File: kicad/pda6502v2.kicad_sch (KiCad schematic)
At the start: 87 parts, among them J1 GPIO1, J2 GPIO2, J3 UART, J4 Screw_Terminal_01x02, J5 Conn_02x04_Odd_Even, J6 ICSP, J7 SPI, J8 FPGA_EXT, J9 SID, SW1 SW_Push, SW2 SW_Push, U1 W65C02SxP, U10 LT3030, U11 SC28L92A1B, U2 W65C22SxP, U3 W65C22SxP, U4 DS1818, U5 AS6C4008-55PCN, U6 ARMSID, U7 AT25M01, U8 ICE40HX4K-TQ144, U9 TLV1117-33, X1 8 MHz, X2 3.6864 MHz

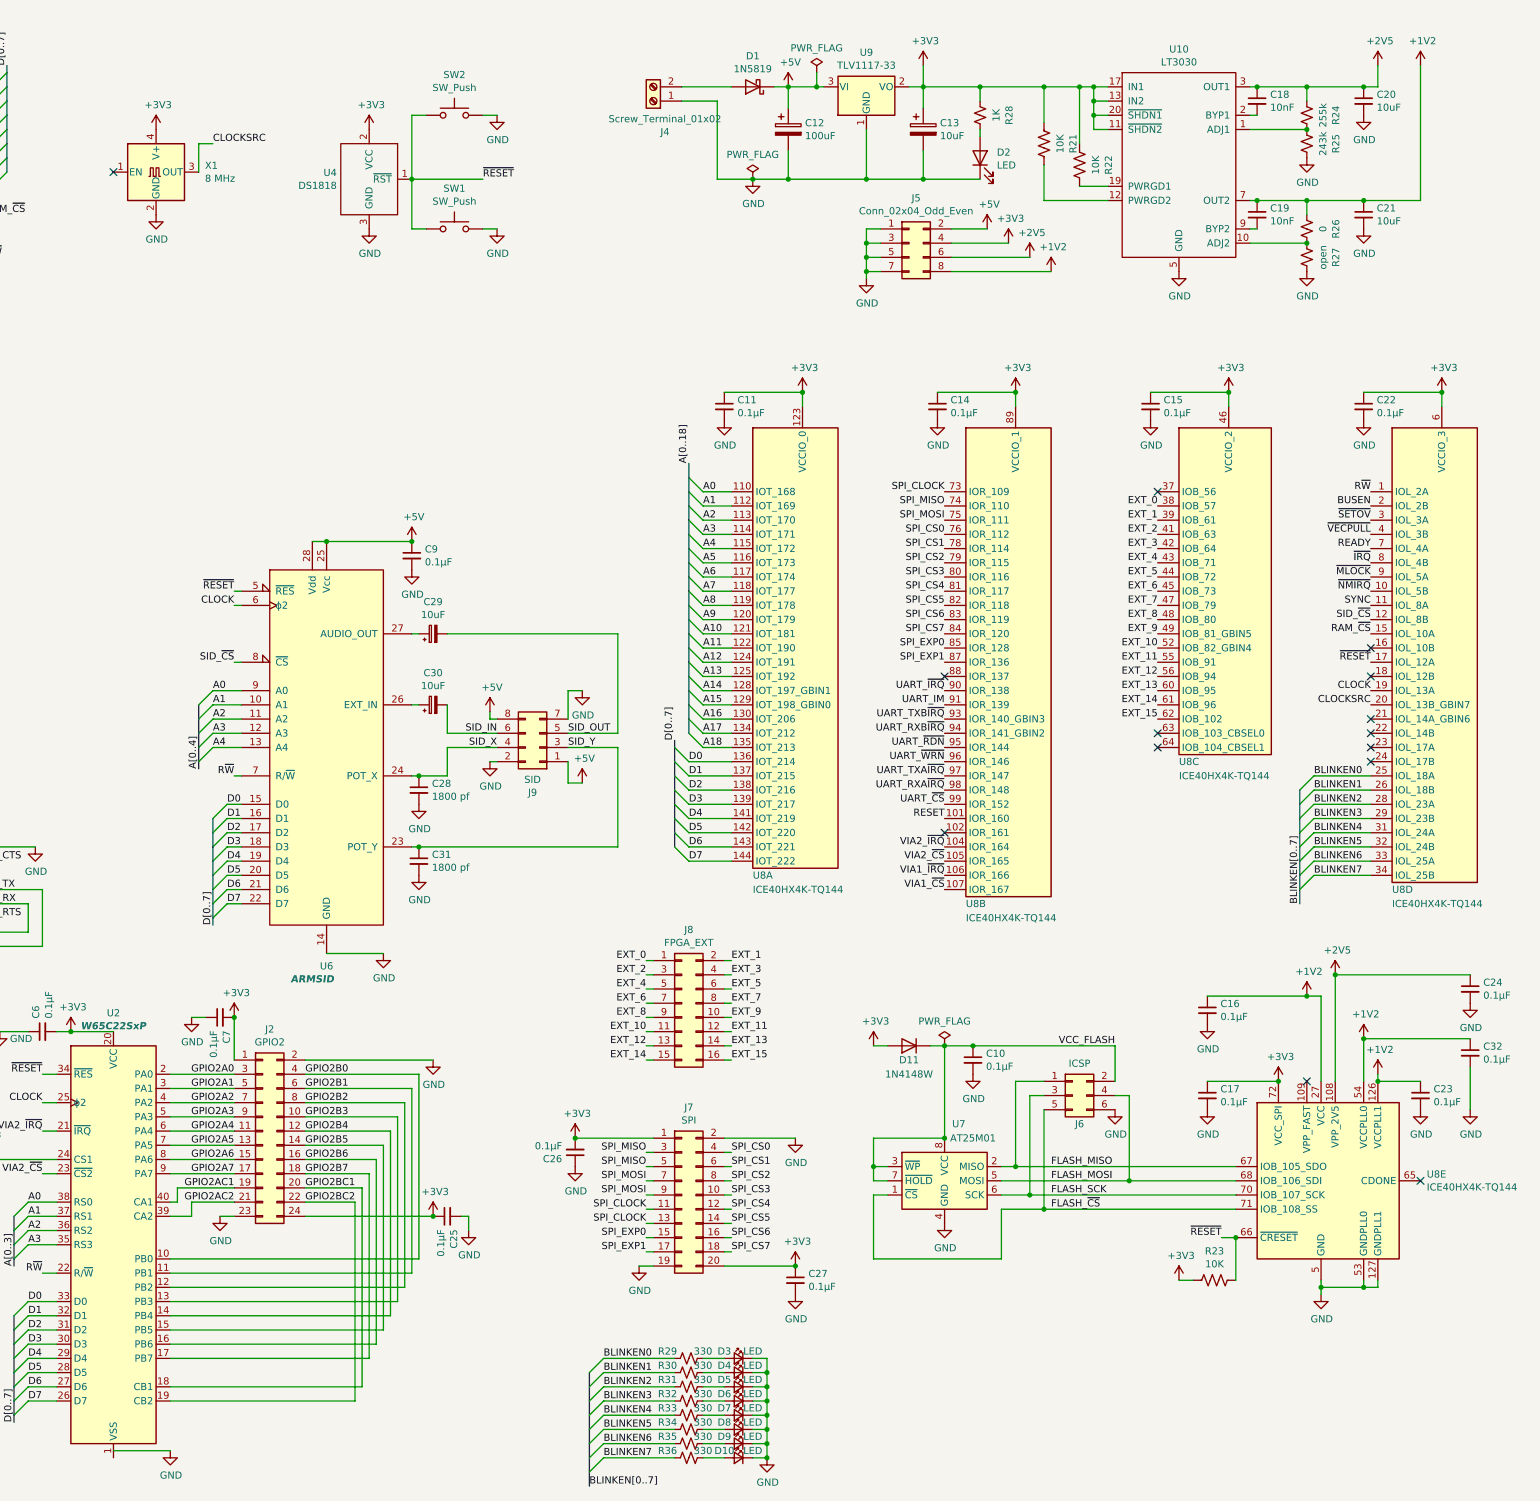
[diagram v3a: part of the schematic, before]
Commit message: kicad: schematic Electrical Rules Checker all fixed
Mostly involved unstacking invisible duplicate power pins on the LM3030
vreg, because the labels (IN1, IN2) of the invisible power pins get
inherited by the net connected to +3V3 which causes the net to have
multiple names; a harmless warning.

The four GND pins can stay invisible-stacked because they have the same
name as the GND net.
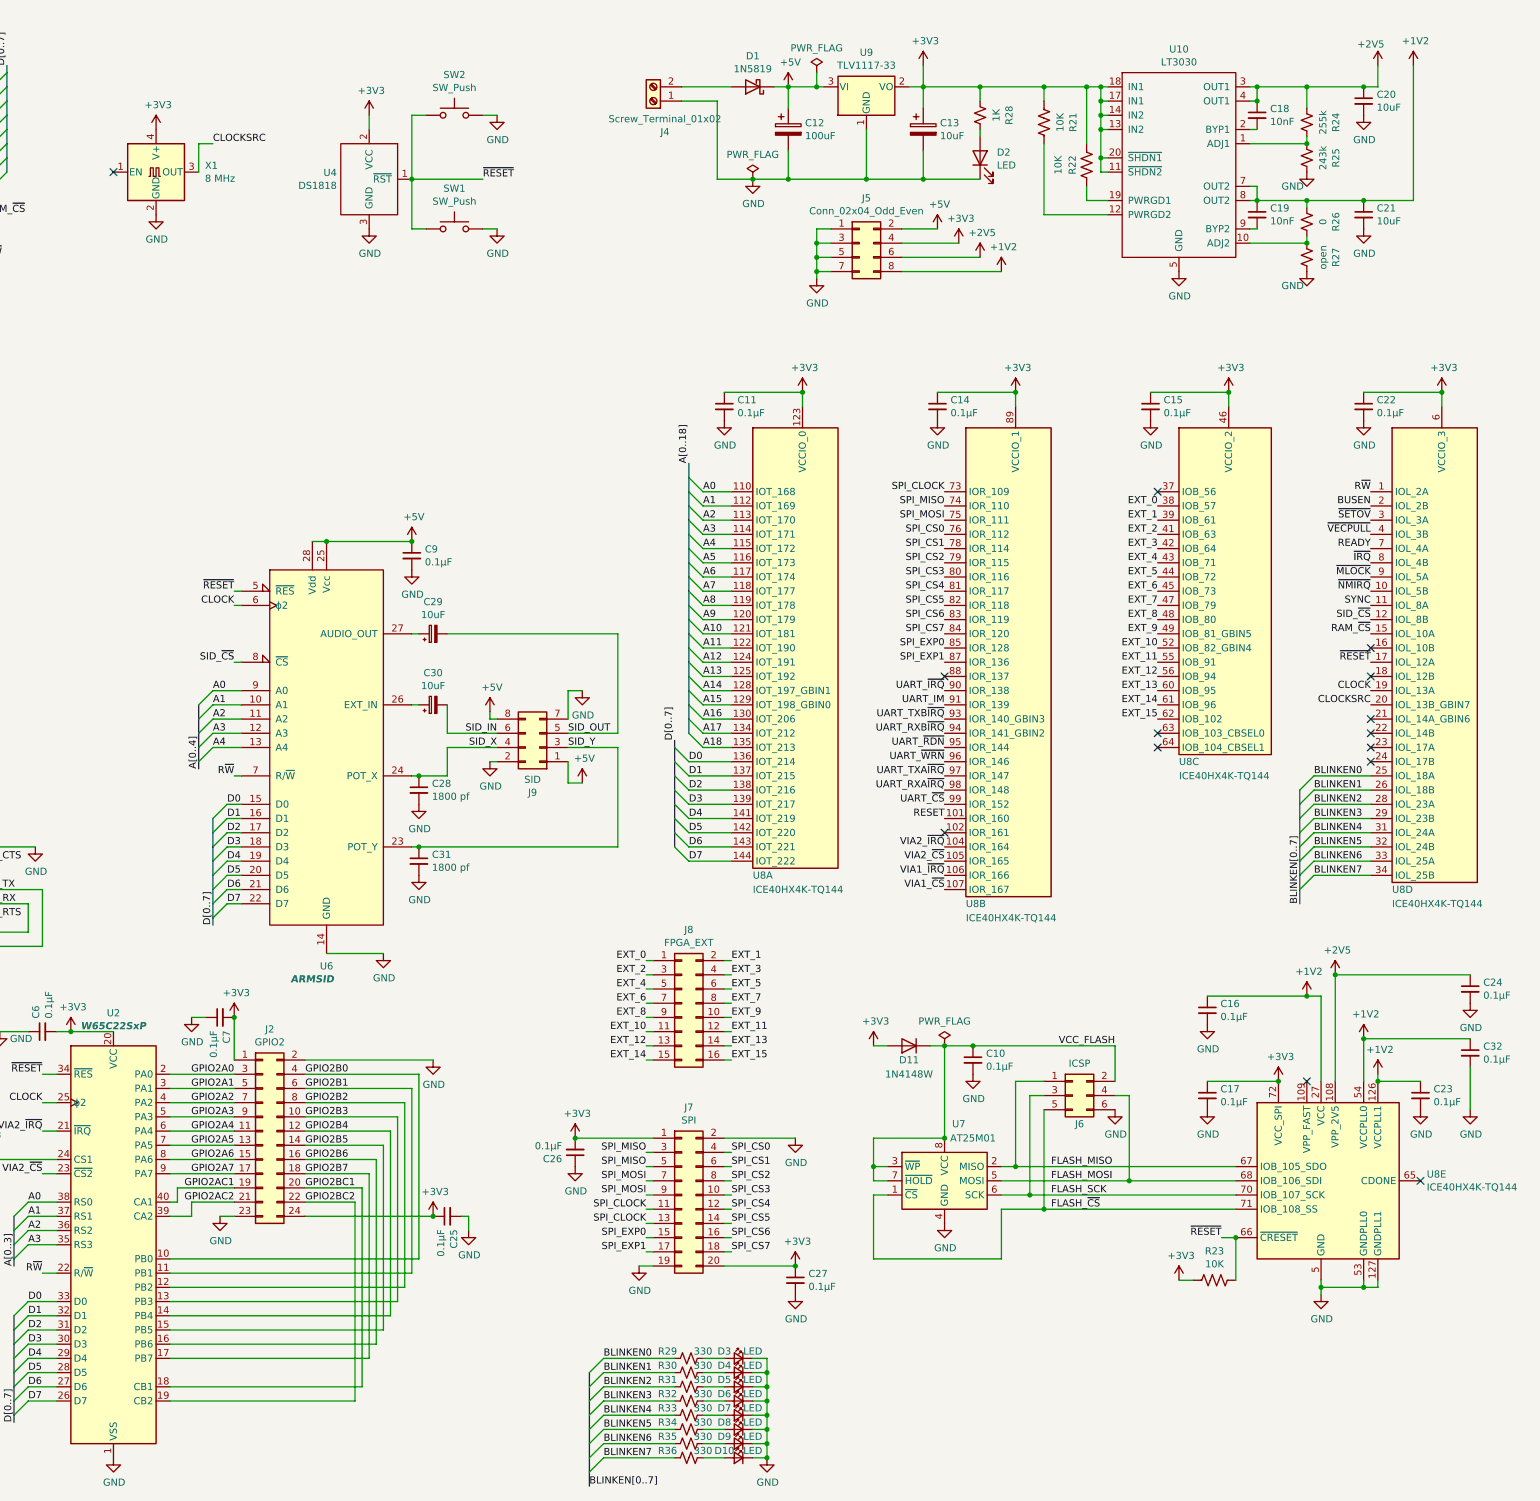
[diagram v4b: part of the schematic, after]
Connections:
- net GND: now also U2.1 (VSS)
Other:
- moved on the sheet: C18, J5, R21, R22, R24, R25, R26
